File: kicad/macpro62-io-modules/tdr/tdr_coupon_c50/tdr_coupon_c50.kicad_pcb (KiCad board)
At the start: 2 copper layers, 58 x 29 mm, 10 parts

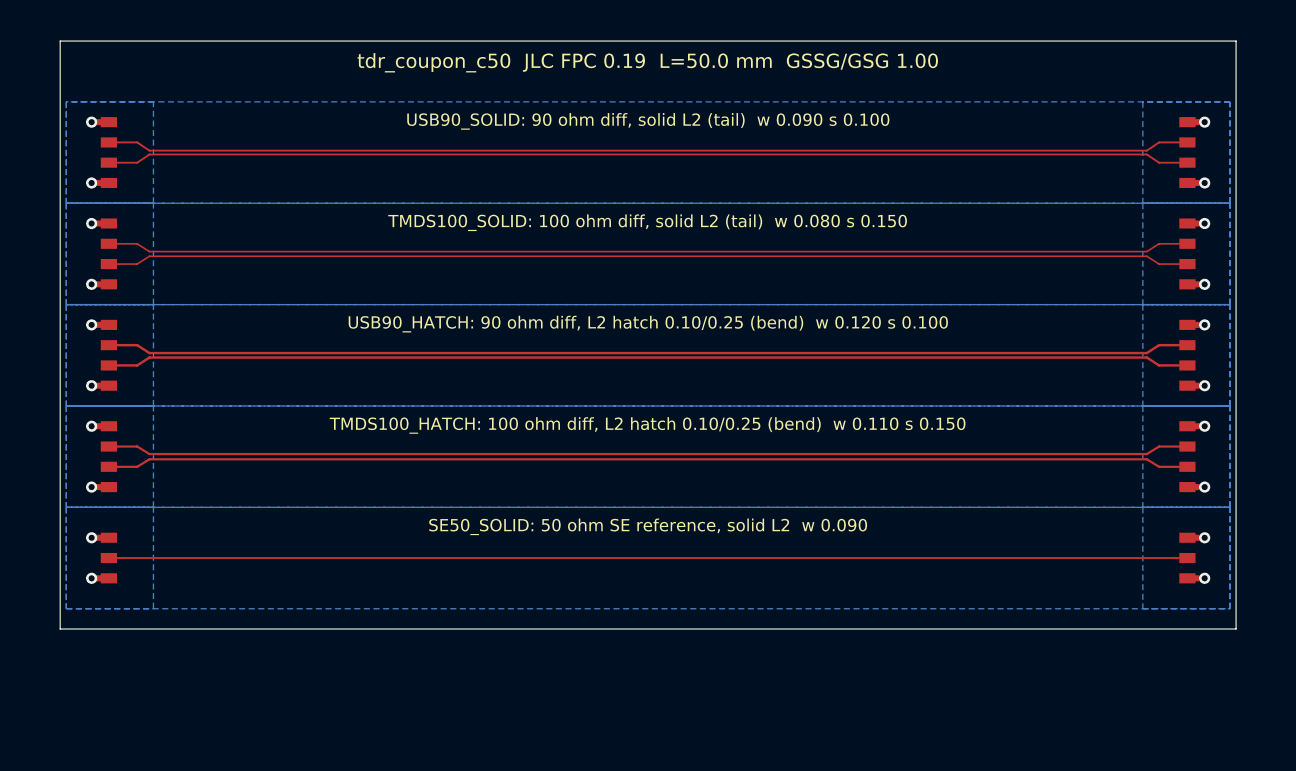
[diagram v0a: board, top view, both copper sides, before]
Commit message: USB-C flex module routed (HYCW417, 0 DRC, matched pairs), 3-mil min on flexes, two flex panels, CH334F + ASM1182e QFN-48 footprints
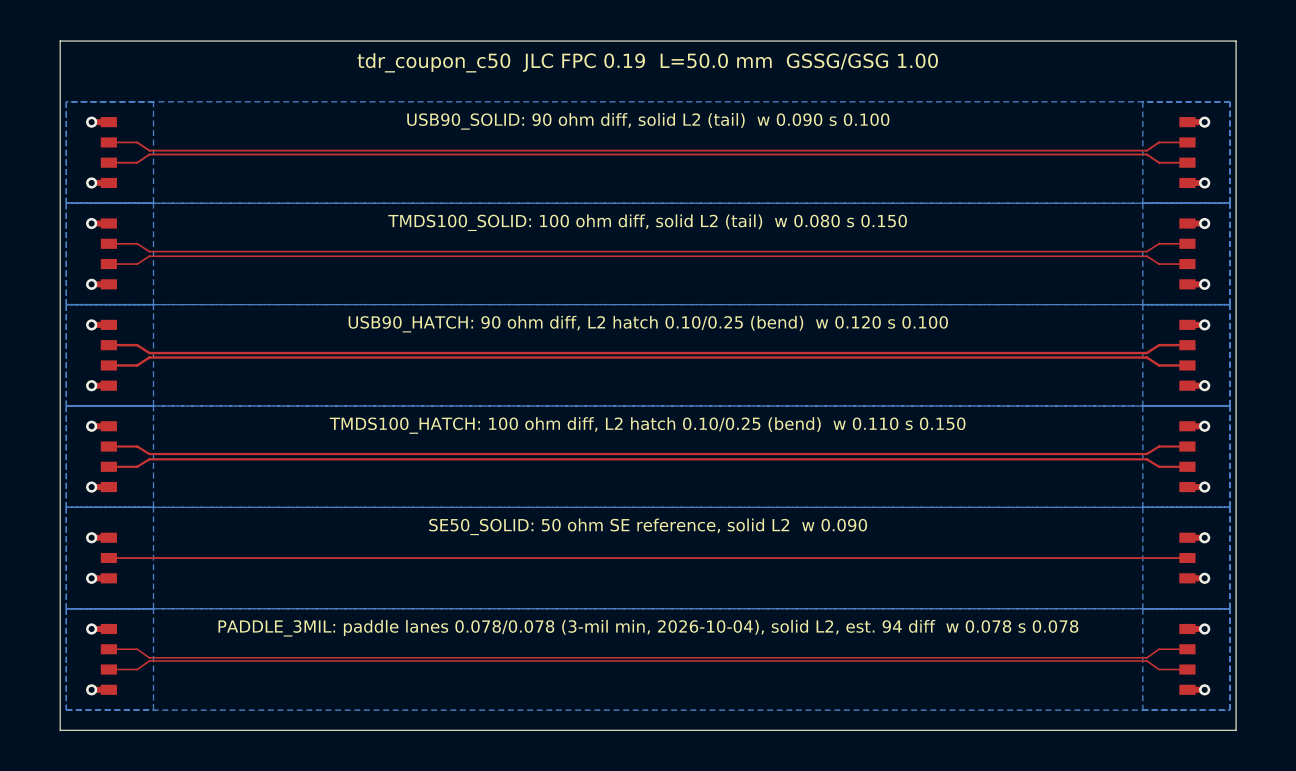
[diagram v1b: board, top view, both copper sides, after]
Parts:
- added TP6A: TDR_LAUNCH, , F.Cu at (102.4, 130.5)
- added TP6B: TDR_LAUNCH, , F.Cu at (155.6, 130.5)
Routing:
- net PADDLE_3MIL_P: track 0.00 -> 52.7 mm
- net PADDLE_3MIL_N: track 0.00 -> 52.7 mm
- net GND: track 17.0 -> 20.4 mm, vias 20 -> 24
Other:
- board size 58 x 29 mm -> 58 x 34 mm
- board text added: "PADDLE_3MIL: paddle lanes 0.078/0.078 (3-mil min, 2026-10-04), solid L2, est. 94 diff w 0.078 s 0.078"
